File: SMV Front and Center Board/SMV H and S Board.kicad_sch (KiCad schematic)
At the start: 14 parts, among them J1 XT60-M, J2 XT60-M, J3 XT60-M, J4 XT60-M, J5 XT60-M, J6 XT60-M, Q1 PSMN1R8-40YLC_115 - MOSFET, Q3 PSMN1R8-40YLC_115 - MOSFET, U2 TLV76650QWDRBRQ1 (16V->5V), U3 PADS131M04QPWRQ1

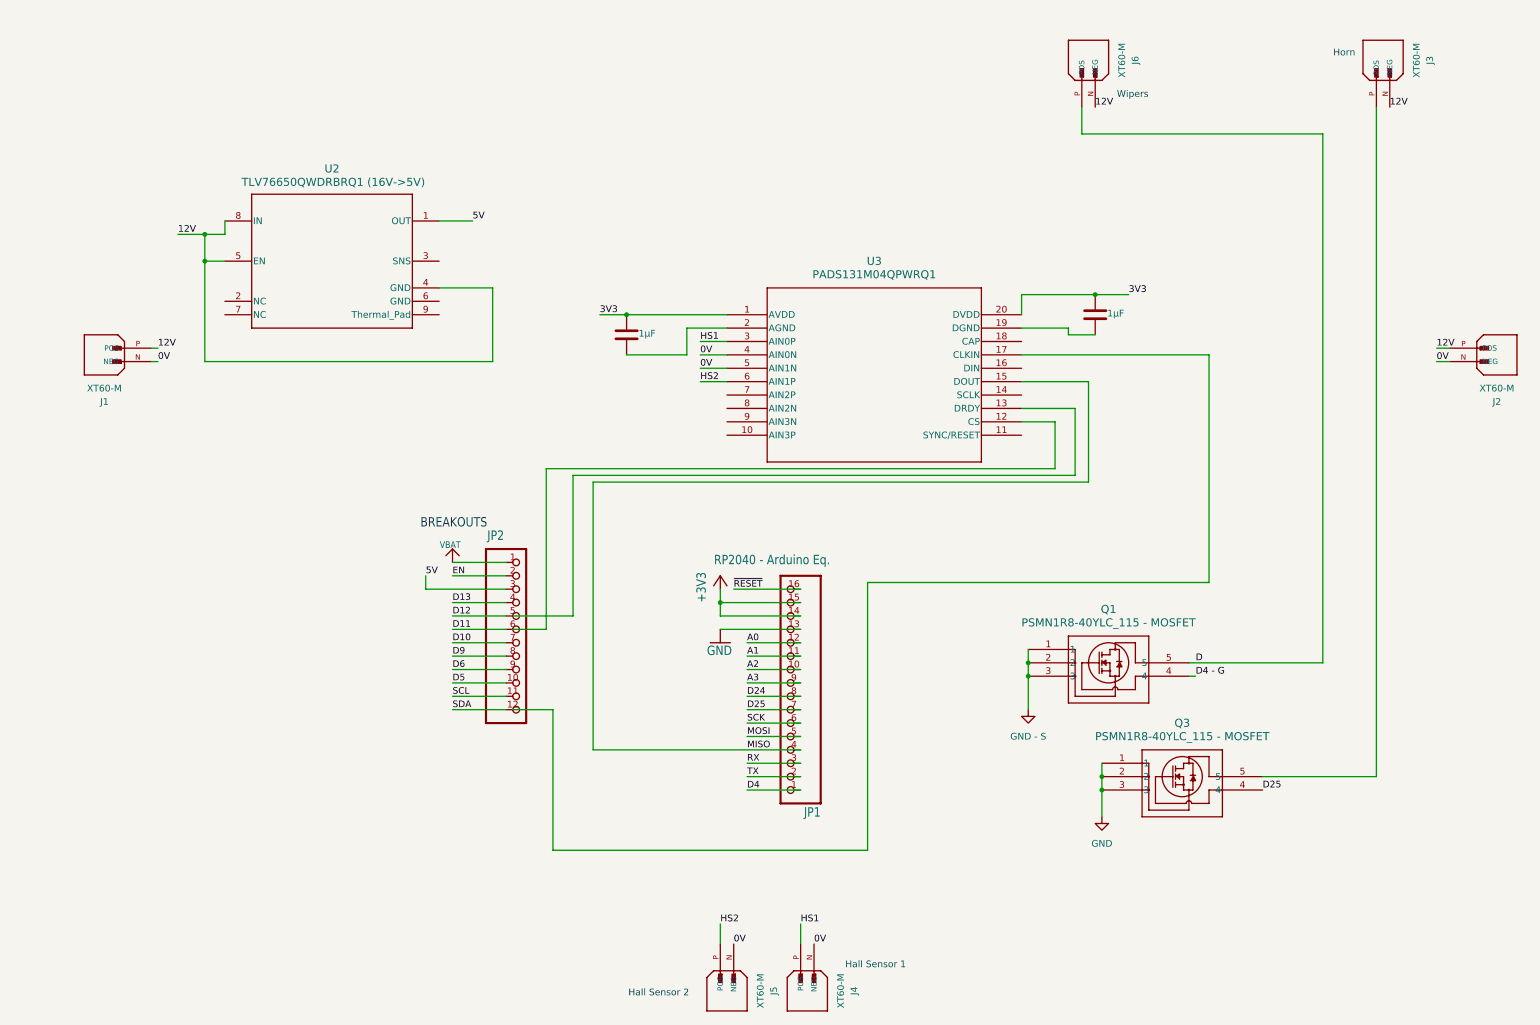
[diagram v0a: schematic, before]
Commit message: Reorganied RPS2040 and ADC
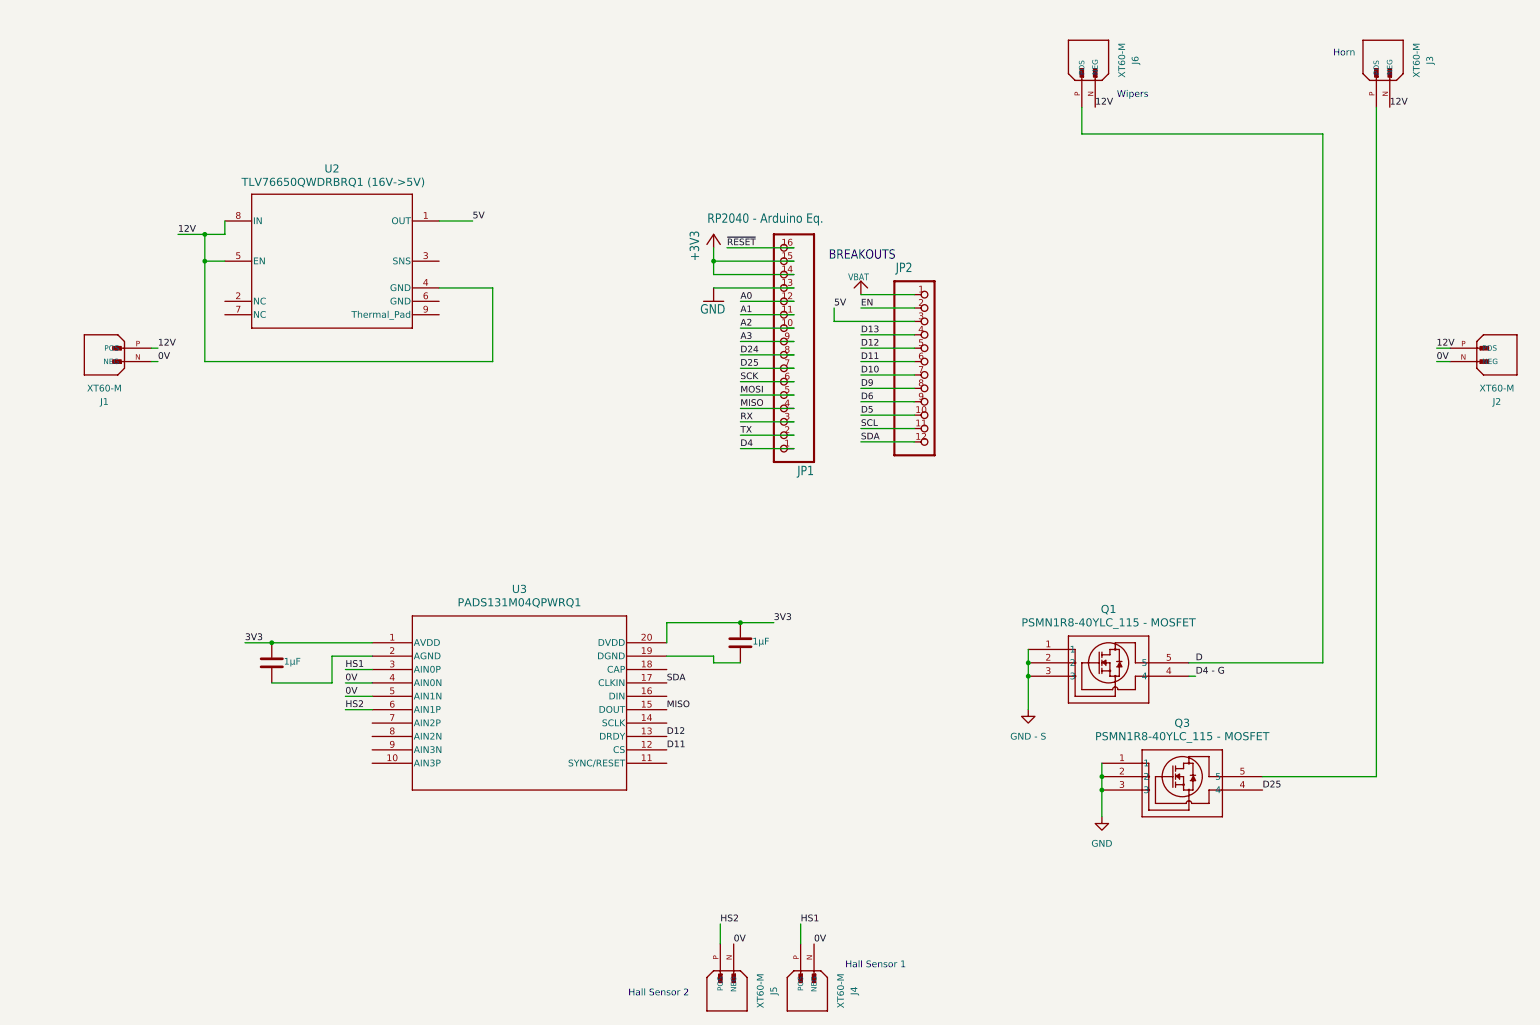
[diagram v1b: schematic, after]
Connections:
- net D11: now also U3.12 (CS)
- net D12: now also U3.13 (DRDY)
- net SDA: now also U3.17 (CLKIN)
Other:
- moved on the sheet: JP1, JP2, U3

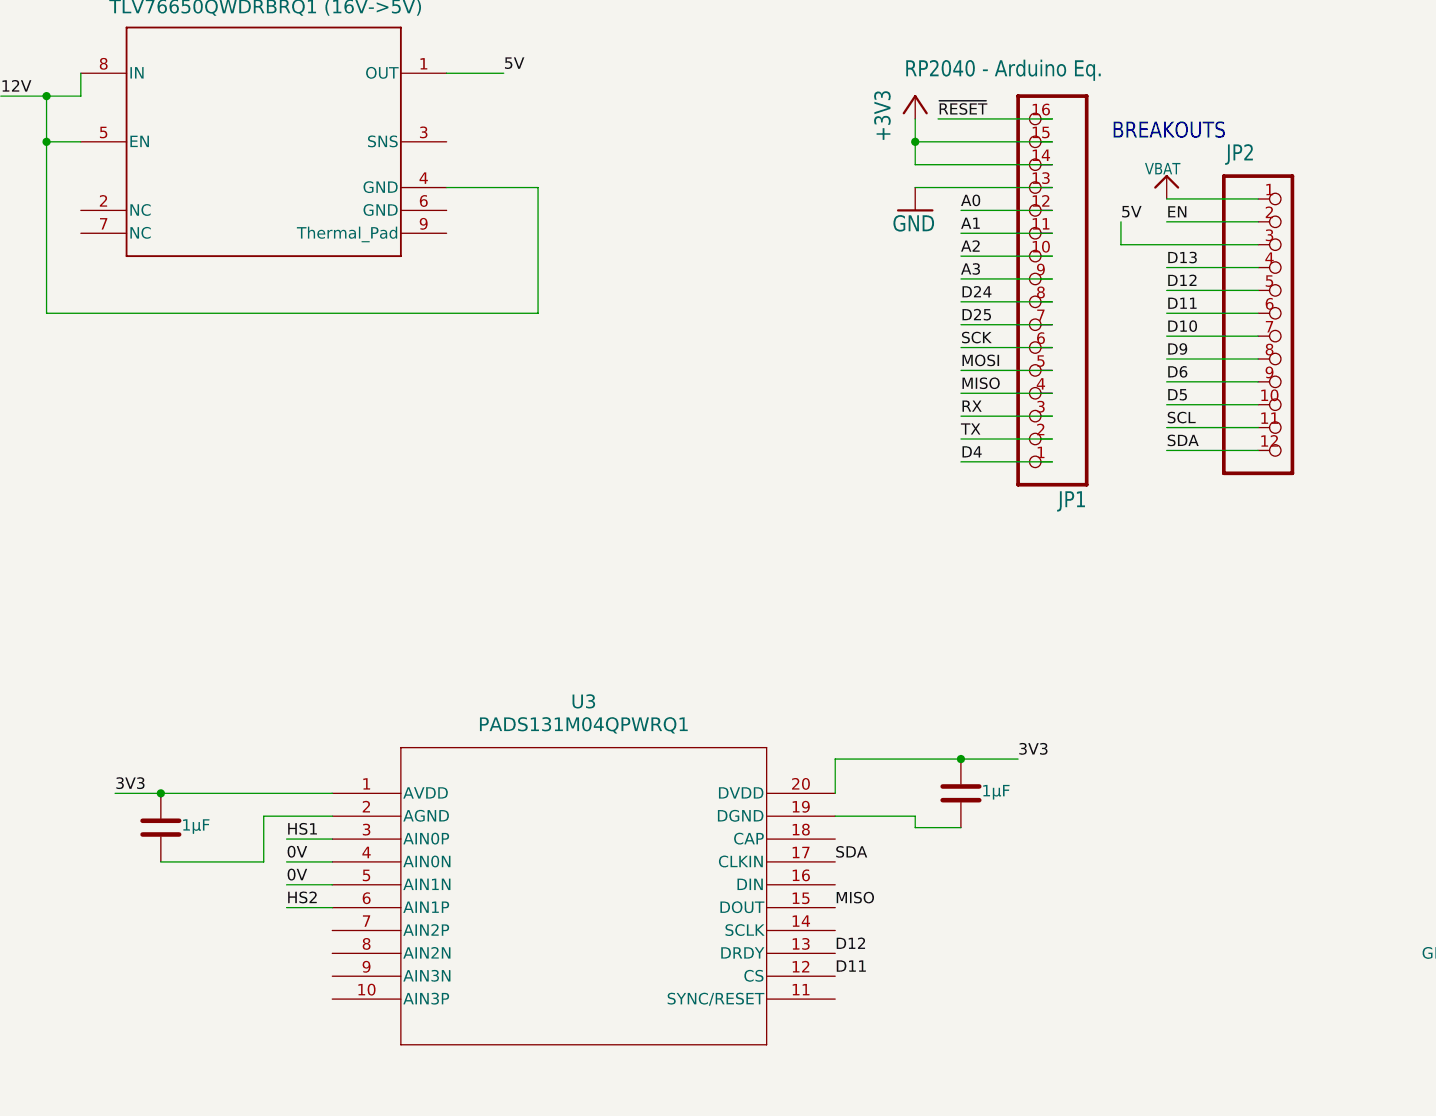
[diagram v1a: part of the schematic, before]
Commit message: Added necessary grounds and rearranged components. Traces have been limited to node labels for now.
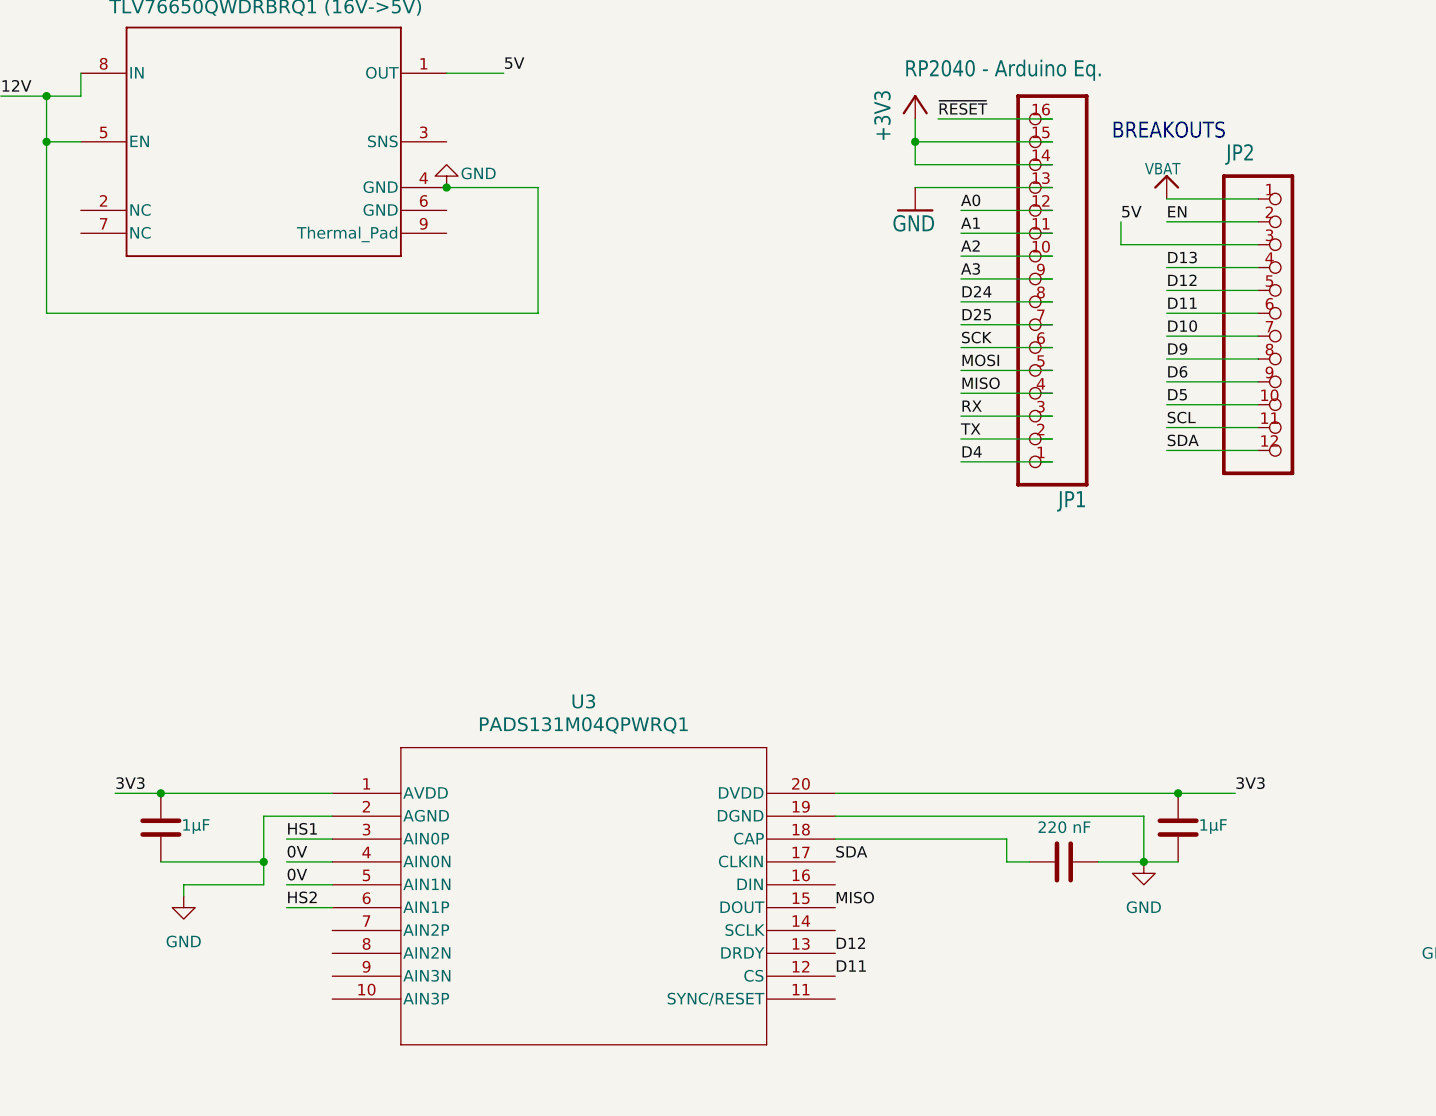
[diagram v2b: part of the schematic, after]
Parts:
- added C3: 220 nF, symbol Device:C
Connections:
- net 12V is gone; now on net GND: J1.P (POS), J2.P (POS), J3.N (NEG), J6.N (NEG), U2.4 (GND), U2.5 (EN), U2.8 (IN)
- net GND: now also C1.2, C2.2, U3.19 (DGND), U3.2 (AGND), C3.2
- net at U3.18 (CAP): now also C3.1
